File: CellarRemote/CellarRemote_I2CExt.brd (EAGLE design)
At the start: 30.5 x 38.1 mm, 19 parts, among them M1 BSS84

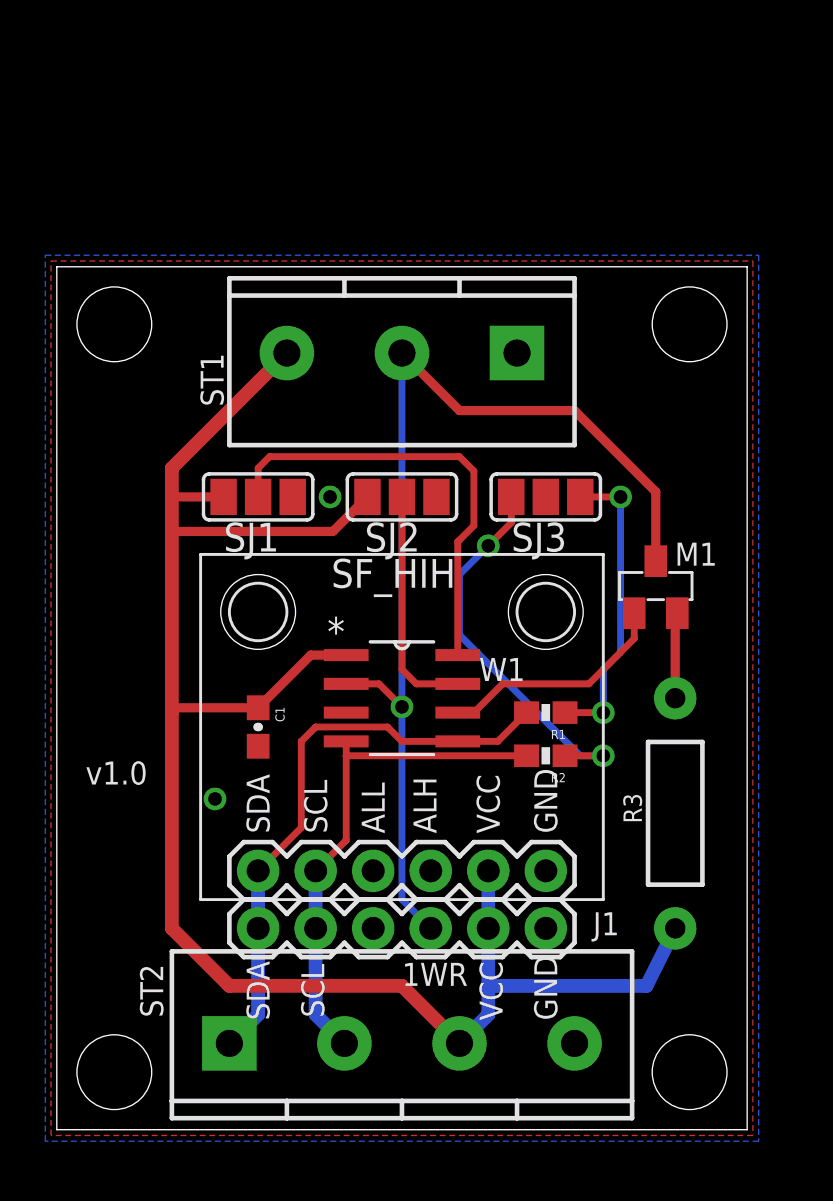
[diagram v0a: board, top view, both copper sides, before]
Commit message: Added CellarRemote_I2CExt
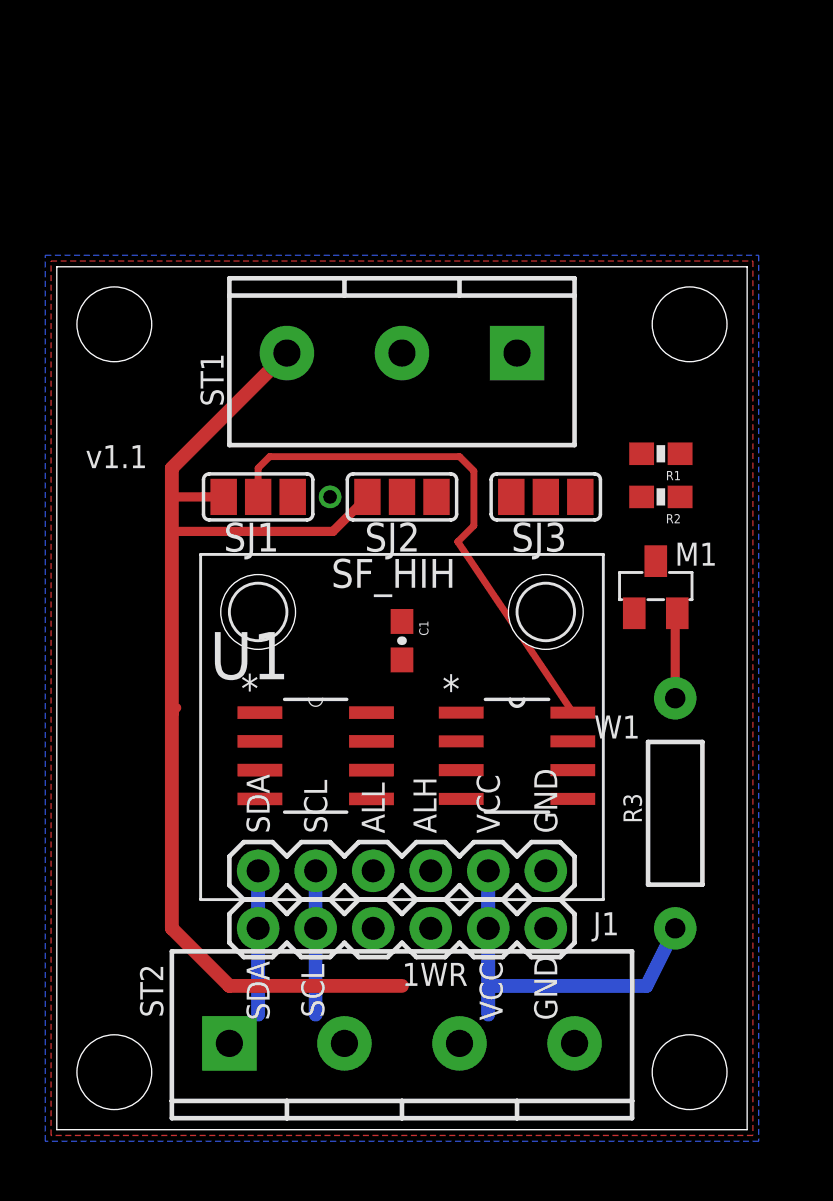
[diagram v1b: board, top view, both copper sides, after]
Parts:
- added U1: P82B715D, Texas Instruments_By_element14_Batch_1:SOIC127P600X175-8N
- moved R1 12.5 mm to (26.7, 29.8)
- moved R2 12.5 mm to (26.7, 27.9)
- moved C1 7.41 mm to (15.2, 21.6)
- moved W1 5.68 mm to (20.3, 16.5)
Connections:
- new net N$4: ST2.3, U1.2
- new net N$5: ST2.4, U1.7
- net GND: now also ST2.2, U1.4; no longer ST2.4
- net SCL: now also U1.3; no longer ST2.2
- net SDA: now also U1.6; no longer ST2.1
- net VCC: now also ST2.1, U1.8; no longer ST2.3
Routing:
- net 1WR: track 45.6 -> 0.00 mm, vias 1 -> 0
- net SDA: track 25.6 -> 6.35 mm
- net N$3: track 17.3 -> 0.00 mm, vias 2 -> 0
- net SCL: track 22.4 -> 6.35 mm
- net VCC: track 80.6 -> 66.7 mm
- net N$2: track 13.6 -> 0.00 mm, vias 2 -> 0
- net AD1: track 10.3 -> 0.00 mm
- net N$1: track 10.3 -> 0.00 mm
- net AD0: track 19.7 -> 23.8 mm
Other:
- board text added: "v1.1"
- board text removed: "v1.0"

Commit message: Added Raspberry pi board, updated I2C extender pullup resistors to other boards
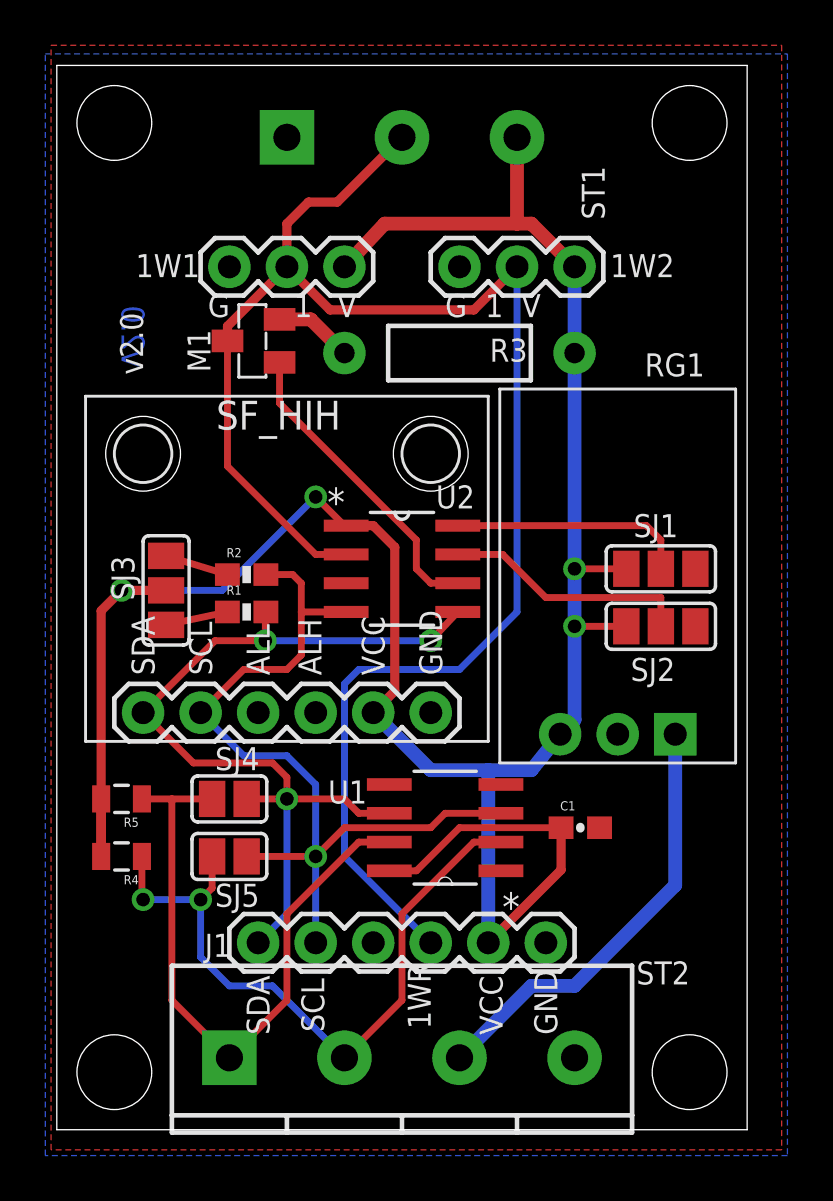
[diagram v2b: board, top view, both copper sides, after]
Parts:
- removed W1: DS2482-100, PuffinOneWIre:SOIC8
- added 1W1, 1W2: (no value), SparkFun-Connectors:1X03
- added R4, R5: (no value), SparkFun-Resistors:0805
- added RG1: 3v3, Puffin:MURATA_REG_HOR
- added SJ4, SJ5: (no value), jumper:SJ
- added U2: DS2482-100, PuffinOneWIre:SOIC8
- moved R3 22.4 mm to (17.8, 34.3), turned to 0 degrees
- moved M1 20.8 mm to (8.64, 34.8), turned to 90 degrees
- moved R1 19.6 mm to (8.38, 22.9), turned to 0 degrees
- moved R2 18.6 mm to (8.38, 24.5), turned to 0 degrees
- moved SJ1 18.1 mm to (26.7, 24.8)
- moved SJ3 17.3 mm to (4.83, 23.8), turned to 270 degrees
- moved ST1 13.9 mm to (10.2, 43.8), flipped to the bottom
- moved SJ2 12.8 mm to (26.7, 22.2)
- moved C1 11.4 mm to (23.1, 13.3), turned to 0 degrees
- moved U$3 8.89 mm to (27.9, 44.5)
- moved U$4 8.89 mm to (2.54, 44.5)
- moved SF_HIH 8.64 mm to (10.2, 18.4)
- moved U$6 8.64 mm to (3.81, 29.8)
- moved U$7 8.64 mm to (16.5, 29.8)
- moved U1 6.54 mm to (17.1, 13.3), turned to 180 degrees
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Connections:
- new net 12V: RG1.1, ST2.3
- net 1WR: now also 1W1.2, 1W2.2, U2.2; no longer W1.2
- net AD0: now also U2.8; no longer W1.8
- net AD1: now also U2.7; no longer W1.7
- net GND: now also 1W1.1, 1W2.1, RG1.2, ST2.4, U2.3; no longer ST2.2, W1.3
- net N$1: now also U2.6; no longer W1.6
- net N$4: now also R4.1, SJ5.1, ST2.2; no longer ST2.3
- net N$5: now also R5.1, SJ4.1, ST2.1; no longer ST2.4
- net SCL: now also SJ5.2, U2.4; no longer W1.4
- net SDA: now also SJ4.2, U2.5; no longer W1.5
- net VCC: now also 1W1.3, 1W2.3, R4.2, R5.2, RG1.3, U2.1; no longer ST2.1, W1.1
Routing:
- net 1WR: track 0.00 -> 74.2 mm
- net VCC: track 66.7 -> 112.6 mm, vias 0 -> 4
- net SDA: track 6.35 -> 39.0 mm, vias 0 -> 3
- net SCL: track 6.35 -> 37.9 mm, vias 0 -> 1
- net N$4: track 0.00 -> 30.4 mm, vias 0 -> 2
- net N$5: track 0.00 -> 28.8 mm
- net 12V: track 0.00 -> 19.3 mm
- net N$1: track 0.00 -> 13.7 mm
- net AD0: track 23.8 -> 10.5 mm
- net AD1: track 0.00 -> 11.0 mm
- net N$3: track 0.00 -> 2.83 mm
- net N$2: track 0.00 -> 2.77 mm
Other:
- board size 30.5 x 38.1 mm -> 30.5 x 47 mm
- board text added: "1"
- board text added: "G"
- board text added: "G 1 V"
- board text added: "V"
- board text added: "v2.0"
- board text removed: "v1.1"

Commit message: Tweaks to cellar remote board
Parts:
- moved RG1 0.95 mm to (24.8, 18.4), flipped to the bottom
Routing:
- net VCC: track 112.6 -> 119.7 mm
- net 12V: track 19.3 -> 21.4 mm
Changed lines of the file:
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@@
 </element>
 <element name="SJ3" library="jumper" package="SJ_2" value="" x="4.826" y="23.8125" smashed="yes" rot="R270">
-<attribute name="NAME" x="2.413" y="25.3365" size="1.016" layer="25" font="vector" ratio="15" rot="R270"/>
+<attribute name="NAME" x="2.7305" y="26.924" size="1.016" layer="25" font="vector" ratio="15" rot="R270"/>
 <attribute name="VALUE" x="4.826" y="23.9126" size="0.02" layer="27" rot="R270"/>
 </element>
@@
 <element name="R4" library="SparkFun-Resistors" package="0805" value="" x="2.8575" y="12.065" rot="R180"/>
 <element name="R5" library="SparkFun-Resistors" package="0805" value="" x="2.8575" y="14.605" rot="R180"/>
-<element name="RG1" library="Puffin" package="MURATA_REG_HOR" value="3v3" x="24.765" y="17.4625" smashed="yes">
-<attribute name="NAME" x="25.9588" y="33.2613" size="1.016" layer="25" font="vector" ratio="15"/>
-<attribute name="VALUE" x="23.495" y="29.5275" size="1.016" layer="27" font="vector" ratio="15"/>
+<element name="RG1" library="Puffin" package="MURATA_REG_HOR" value="3v3" x="24.765" y="18.415" smashed="yes" rot="MR0">
+<attribute name="NAME" x="27.3812" y="34.2138" size="1.016" layer="26" font="vector" ratio="15" rot="MR0"/>
+<attribute name="VALUE" x="26.035" y="30.48" size="1.016" layer="28" font="vector" ratio="15" rot="MR0"/>
 </element>
 </elements>
@@
 <contactref element="R5" pad="2"/>
 <contactref element="RG1" pad="3"/>
-<wire x1="22.225" y1="17.4625" x2="20.955" y2="15.875" width="0.6096" layer="16"/>
-<wire x1="20.955" y1="15.875" x2="19.05" y2="15.875" width="0.6096" layer="16"/>
 <wire x1="19.05" y1="15.875" x2="16.51" y2="15.875" width="0.6096" layer="16"/>
 <wire x1="13.97" y1="18.415" x2="16.51" y2="15.875" width="0.6096" layer="16"/>
@@
 <via x="22.86" y="22.225" extent="1-16" drill="0.6"/>
 <wire x1="22.86" y1="24.765" x2="22.86" y2="34.29" width="0.6096" layer="16"/>
-<wire x1="22.225" y1="17.4625" x2="22.86" y2="18.0975" width="0.6096" layer="16"/>
-<wire x1="22.86" y1="18.0975" x2="22.86" y2="22.225" width="0.6096" layer="16"/>
 <wire x1="13.97" y1="18.415" x2="14.9225" y2="19.3675" width="0.4064" layer="1"/>
 <wire x1="14.9225" y1="19.3675" x2="14.9225" y2="25.7175" width="0.4064" layer="1"/>
@@
 <wire x1="11.43" y1="27.94" x2="7.3025" y2="23.8125" width="0.3048" layer="16"/>
 <wire x1="7.3025" y1="23.8125" x2="2.8575" y2="23.8125" width="0.3048" layer="16"/>
+<wire x1="27.305" y1="18.415" x2="24.765" y2="15.875" width="0.6096" layer="16"/>
+<wire x1="24.765" y1="15.875" x2="19.05" y2="15.875" width="0.6096" layer="16"/>
+<wire x1="27.305" y1="18.415" x2="25.4" y2="20.32" width="0.6096" layer="1"/>
+<wire x1="25.4" y1="20.32" x2="23.495" y2="20.32" width="0.6096" layer="1"/>
+<wire x1="23.495" y1="20.32" x2="22.86" y2="20.955" width="0.6096" layer="1"/>
+<wire x1="22.86" y1="20.955" x2="22.86" y2="22.225" width="0.6096" layer="1"/>
 </signal>
 <signal name="GND">
@@
 <contactref element="ST2" pad="3"/>
 <contactref element="RG1" pad="1"/>
-<wire x1="17.78" y1="3.175" x2="20.955" y2="6.35" width="0.6096" layer="16"/>
-<wire x1="20.955" y1="6.35" x2="22.86" y2="6.35" width="0.6096" layer="16"/>
-<wire x1="22.86" y1="6.35" x2="27.305" y2="10.795" width="0.6096" layer="16"/>
-<wire x1="27.305" y1="10.795" x2="27.305" y2="17.4625" width="0.6096" layer="16"/>
+<wire x1="17.78" y1="3.175" x2="20.6375" y2="6.0325" width="0.6096" layer="1"/>
+<wire x1="20.6375" y1="6.0325" x2="22.5425" y2="6.0325" width="0.6096" layer="1"/>
+<wire x1="22.5425" y1="6.0325" x2="26.035" y2="9.525" width="0.6096" layer="1"/>
+<wire x1="26.035" y1="9.525" x2="26.035" y2="14.605" width="0.6096" layer="1"/>
+<wire x1="26.035" y1="14.605" x2="22.225" y2="18.415" width="0.6096" layer="1"/>
 </signal>
 </signals>

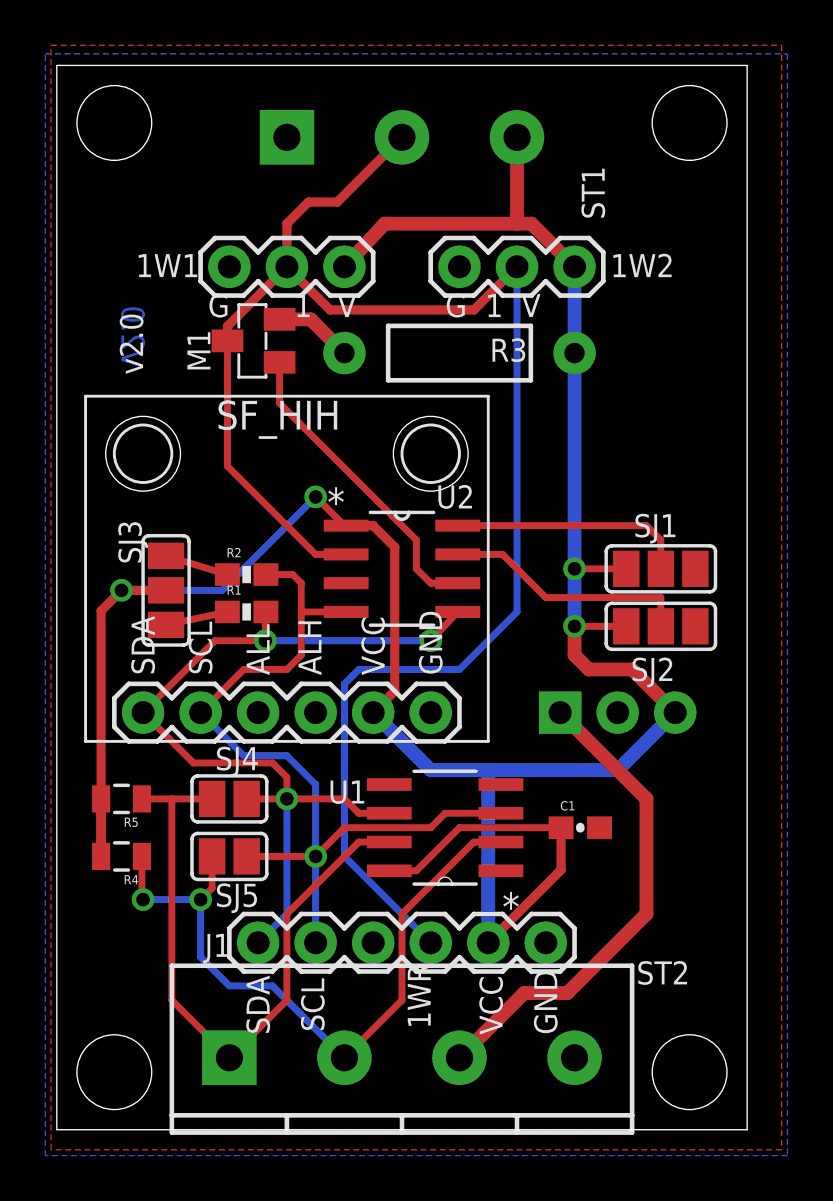
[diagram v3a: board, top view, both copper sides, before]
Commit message: Ver 2 of CellarRemote with I2C extender
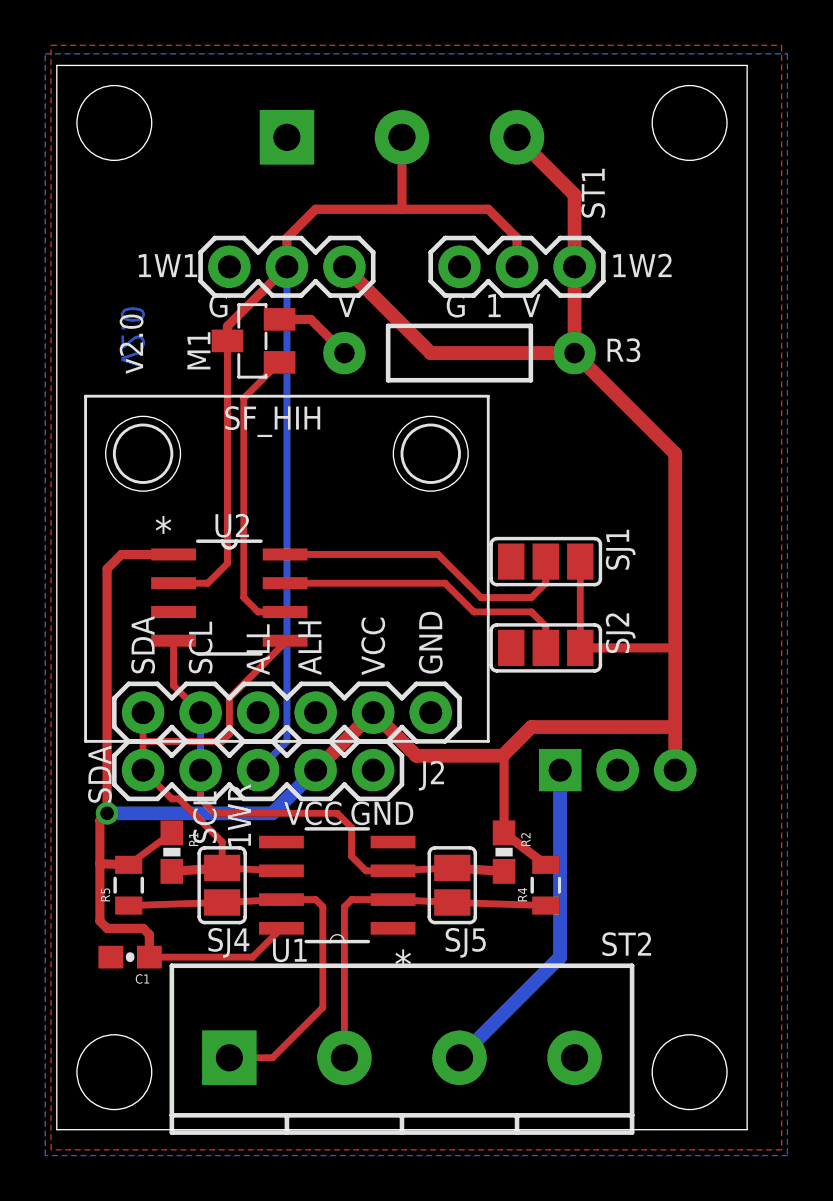
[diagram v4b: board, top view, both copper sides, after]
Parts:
- removed J1: (no value), SparkFun-Connectors:1X06
- removed SJ3: (no value), jumper:SJ_2
- added J2: (no value), SparkFun-Connectors:1X05
- moved C1 20.7 mm to (3.24, 7.62), turned to 180 degrees
- moved R4 18.8 mm to (21.6, 10.8), turned to 90 degrees
- moved R2 16.7 mm to (19.7, 12.3), turned to 270 degrees
- moved R1 11.1 mm to (5.08, 12.3), turned to 270 degrees
- moved SJ5 9.92 mm to (17.5, 10.8), turned to 90 degrees
- moved U2 7.73 mm to (7.62, 23.5)
- moved U1 5.40 mm to (12.4, 10.8)
- moved SJ2 5.17 mm to (21.6, 21.3), turned to 180 degrees
- moved SJ1 5.09 mm to (21.6, 25.1), turned to 180 degrees
- moved R5 3.82 mm to (3.17, 10.8), turned to 90 degrees
- moved SJ4 3.82 mm to (7.30, 10.8), turned to 90 degrees
- moved RG1 2.54 mm to (24.8, 15.9)
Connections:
- removed net N$2: R1.1, SJ3.3
- removed net N$3: R2.1, SJ3.1
- net 1WR: now also J2.3; no longer J1.3
- net GND: now also J2.1; no longer J1.1
- net SCL: now also J2.4; no longer J1.5
- net SDA: now also J2.5; no longer J1.6
- net VCC: now also J2.2, R1.1, R2.1; no longer J1.2, SJ3.2
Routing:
- net 1WR: track 74.2 -> 56.6 mm
- net SDA: track 39.0 -> 22.4 mm, vias 3 -> 0
- net SCL: track 37.9 -> 22.9 mm, vias 1 -> 0
- net N$4: track 30.4 -> 15.7 mm, vias 2 -> 0
- net N$5: track 28.8 -> 18.2 mm
- net 12V: track 21.4 -> 14.5 mm
- net AD0: track 10.5 -> 13.5 mm
- net N$3: track 2.83 -> 0.00 mm
- net VCC: track 119.7 -> 116.9 mm, vias 4 -> 1
- net N$2: track 2.77 -> 0.00 mm
- net AD1: track 11.0 -> 13.2 mm
- net N$1: track 13.7 -> 13.1 mm
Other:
- board text added: "VIN"
- board text removed: "1"
